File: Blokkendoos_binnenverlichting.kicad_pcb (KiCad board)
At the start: 2 copper layers, 206.8 x 26 mm, 104 parts, among them J1 Conn_01x02, J10 Conn_01x04, J11 Conn_01x04, J12 Conn_01x04, J13 Conn_01x04, J14 Conn_01x04, J15 Conn_01x04, J2 Conn_02x11_Counter_Clockwise, J3 Conn_01x04, J4 Conn_01x02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

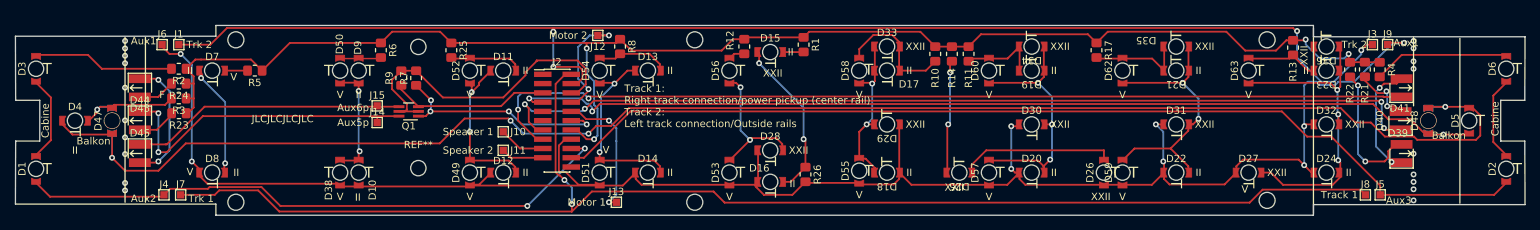
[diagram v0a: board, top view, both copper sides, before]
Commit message: Fixed mounting hole locations and sizes, closes #8
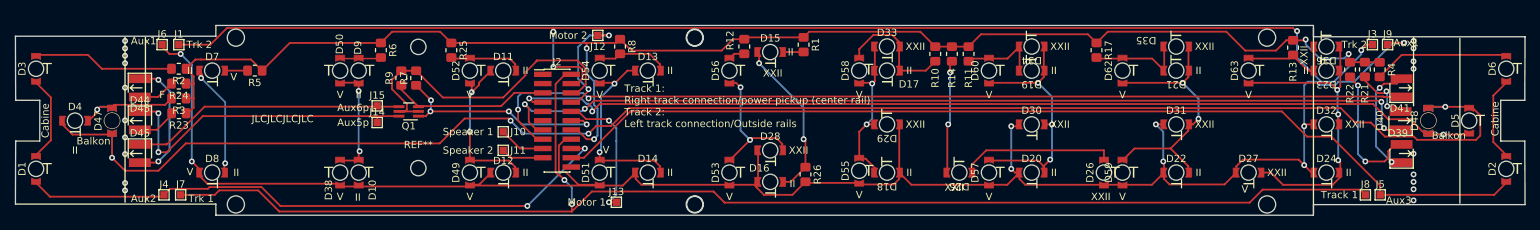
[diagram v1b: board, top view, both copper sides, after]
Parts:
- moved REF** 0.55 mm to (220.5, 138.5)
- moved REF** 0.30 mm to (220.5, 115.6)
- moved REF** 0.30 mm to (79.2, 138.5)
- moved REF** 0.30 mm to (142.1, 138.5)
- moved REF** 0.30 mm to (142.1, 115.6)
- moved REF** 0.30 mm to (79.2, 115.6)
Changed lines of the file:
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@@
   )
   (footprint "MountingHole:MountingHole_2.2mm_M2" locked (layer "F.Cu")
-    (at 220.472 115.922)
+    (at 220.472 115.624)
     (descr "Mounting Hole 2.2mm, no annular, M2")
     (tags "mounting hole 2.2mm no annular m2")
@@
     (fp_circle (center 0 0) (end 2.2 0) (layer "Cmts.User") (width 0.15) (fill none))
     (fp_circle (center 0 0) (end 2.45 0) (layer "F.CrtYd") (width 0.05) (fill none))
-    (pad "" np_thru_hole circle locked (at 0 0) (size 2.2 2.2) (drill 2.2) (layers *.Cu *.Mask))
+    (pad "" np_thru_hole circle locked (at 0 0) (size 2.35 2.35) (drill 2.35) (layers F&B.Cu *.Mask))
   )
   (footprint "Pyth:MHT151CYCT" (layer "F.Cu")
@@
   )
   (footprint "MountingHole:MountingHole_2.2mm_M2" locked (layer "F.Cu")
-    (at 79.192 138.176)
+    (at 79.192 138.474)
     (descr "Mounting Hole 2.2mm, no annular, M2")
     (tags "mounting hole 2.2mm no annular m2")
@@
     (fp_circle (center 0 0) (end 2.2 0) (layer "Cmts.User") (width 0.15) (fill none))
     (fp_circle (center 0 0) (end 2.45 0) (layer "F.CrtYd") (width 0.05) (fill none))
-    (pad "" np_thru_hole circle locked (at 0 0) (size 2.2 2.2) (drill 2.2) (layers *.Cu *.Mask))
+    (pad "" np_thru_hole circle locked (at 0 0) (size 2.35 2.35) (drill 2.35) (layers F&B.Cu *.Mask))
   )
   (footprint "Pyth:MHT151CYCT" (layer "F.Cu")
@@
   )
   (footprint "MountingHole:MountingHole_2.2mm_M2" locked (layer "F.Cu")
-    (at 142.062 138.176)
+    (at 142.062 138.474)
     (descr "Mounting Hole 2.2mm, no annular, M2")
     (tags "mounting hole 2.2mm no annular m2")
@@
     (fp_circle (center 0 0) (end 2.2 0) (layer "Cmts.User") (width 0.15) (fill none))
     (fp_circle (center 0 0) (end 2.45 0) (layer "F.CrtYd") (width 0.05) (fill none))
-    (pad "" np_thru_hole circle locked (at 0 0) (size 2.2 2.2) (drill 2.2) (layers *.Cu *.Mask))
+    (pad "" np_thru_hole circle locked (at 0 0) (size 2.35 2.35) (drill 2.35) (layers F&B.Cu *.Mask))
     (pad "" np_thru_hole circle locked (at 0 0) (size 2.2 2.2) (drill 2.2) (layers *.Cu *.Mask))
   )
@@
   )
   (footprint "MountingHole:MountingHole_2.2mm_M2" locked (layer "F.Cu")
-    (at 142.062 115.922)
+    (at 142.062 115.624)
     (descr "Mounting Hole 2.2mm, no annular, M2")
     (tags "mounting hole 2.2mm no annular m2")
@@
     (fp_circle (center 0 0) (end 2.2 0) (layer "Cmts.User") (width 0.15) (fill none))
     (fp_circle (center 0 0) (end 2.45 0) (layer "F.CrtYd") (width 0.05) (fill none))
-    (pad "" np_thru_hole circle locked (at 0 0) (size 2.2 2.2) (drill 2.2) (layers *.Cu *.Mask))
+    (pad "" np_thru_hole circle locked (at 0 0) (size 2.35 2.35) (drill 2.35) (layers F&B.Cu *.Mask))
     (pad "" np_thru_hole circle locked (at 0 0) (size 2.2 2.2) (drill 2.2) (layers *.Cu *.Mask))
   )
@@
   )
   (footprint "MountingHole:MountingHole_2.2mm_M2" locked (layer "F.Cu")
-    (at 79.192 115.922)
+    (at 79.192 115.624)
     (descr "Mounting Hole 2.2mm, no annular, M2")
     (tags "mounting hole 2.2mm no annular m2")
@@
     (fp_circle (center 0 0) (end 2.2 0) (layer "Cmts.User") (width 0.15) (fill none))
     (fp_circle (center 0 0) (end 2.45 0) (layer "F.CrtYd") (width 0.05) (fill none))
-    (pad "" np_thru_hole circle locked (at 0 0) (size 2.2 2.2) (drill 2.2) (layers *.Cu *.Mask))
+    (pad "" np_thru_hole circle locked (at 0 0) (size 2.35 2.35) (drill 2.35) (layers F&B.Cu *.Mask))
   )
   (footprint "Pyth:MHT151CYCT_dual_side" (layer "F.Cu")
@@
   )
   (footprint "MountingHole:MountingHole_2.2mm_M2" locked (layer "F.Cu")
-    (at 220.472 137.922)
+    (at 220.472 138.474)
     (descr "Mounting Hole 2.2mm, no annular, M2")
     (tags "mounting hole 2.2mm no annular m2")
@@
     (fp_circle (center 0 0) (end 2.2 0) (layer "Cmts.User") (width 0.15) (fill none))
     (fp_circle (center 0 0) (end 2.45 0) (layer "F.CrtYd") (width 0.05) (fill none))
-    (pad "" np_thru_hole circle locked (at 0 0) (size 2.2 2.2) (drill 2.2) (layers *.Cu *.Mask))
+    (pad "" np_thru_hole circle locked (at 0 0) (size 2.35 2.35) (drill 2.35) (layers F&B.Cu *.Mask))
   )
   (footprint "Pyth:MHT151CYCT" (layer "F.Cu")

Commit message: Moved motor car mounting holes, closes #7
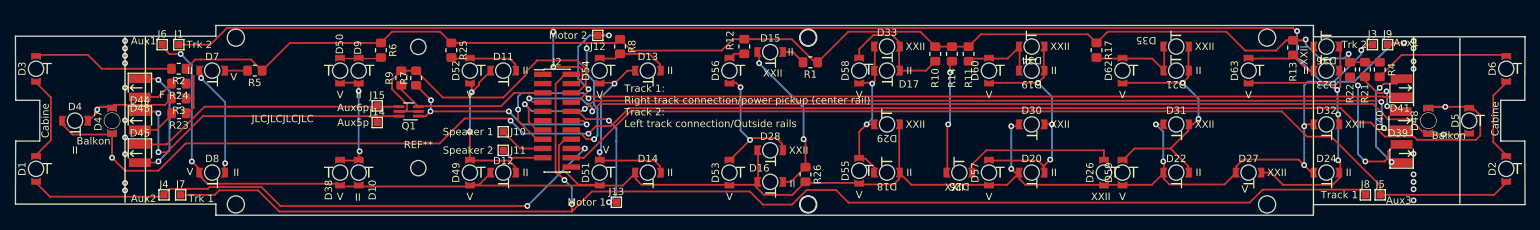
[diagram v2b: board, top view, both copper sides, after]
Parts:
- moved REF** 15.5 mm to (157.6, 138.5)
- moved REF** 15.5 mm to (157.6, 115.6)
- moved R1 2.59 mm to (157.9, 119.0), turned to 180 degrees
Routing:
- net VPP: track 203.4 -> 206.4 mm
- net /Gleis 1: track 187.7 -> 189.4 mm

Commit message: Moved front and rear light, closes #14, moved x less then 1.4 mm, that seems too much.
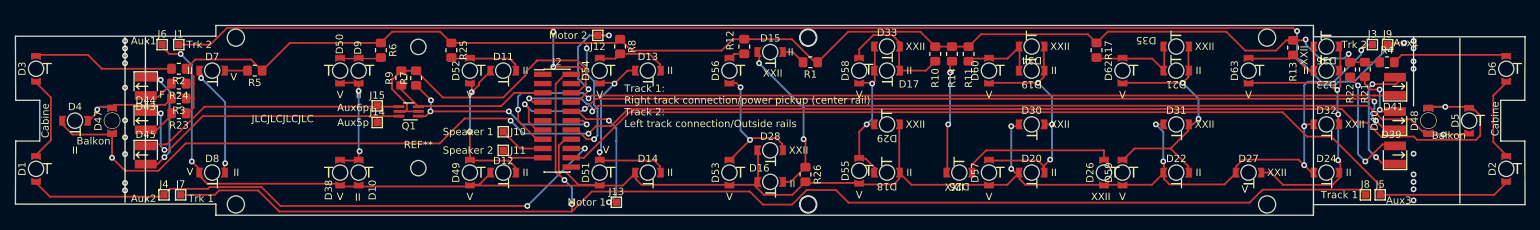
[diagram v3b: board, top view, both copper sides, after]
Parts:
- moved R4 1.41 mm to (236.9, 119.0), turned to 0 degrees
- moved D41 0.92 mm to (238.0, 122.3)
- moved D39 0.92 mm to (238.0, 131.7)
- moved D43 0.82 mm to (66.8, 122.3)
- moved D45 0.82 mm to (66.8, 131.7)
- moved D44 0.80 mm to (66.8, 127.0)
- moved D40 0.76 mm to (238.0, 127.0)
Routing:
- net Net-(D6-Pad2): track 18.6 -> 15.8 mm
- net Net-(D39-Pad1): track 16.2 -> 18.1 mm
- net /Aux5p: track 43.7 -> 42.2 mm
- net /F0r: track 129.6 -> 130.7 mm
- net /F0f: track 129.4 -> 128.5 mm
- net Net-(D43-Pad1): track 17.7 -> 16.8 mm
- net Net-(D39-Pad2): track 18.9 -> 18.4 mm

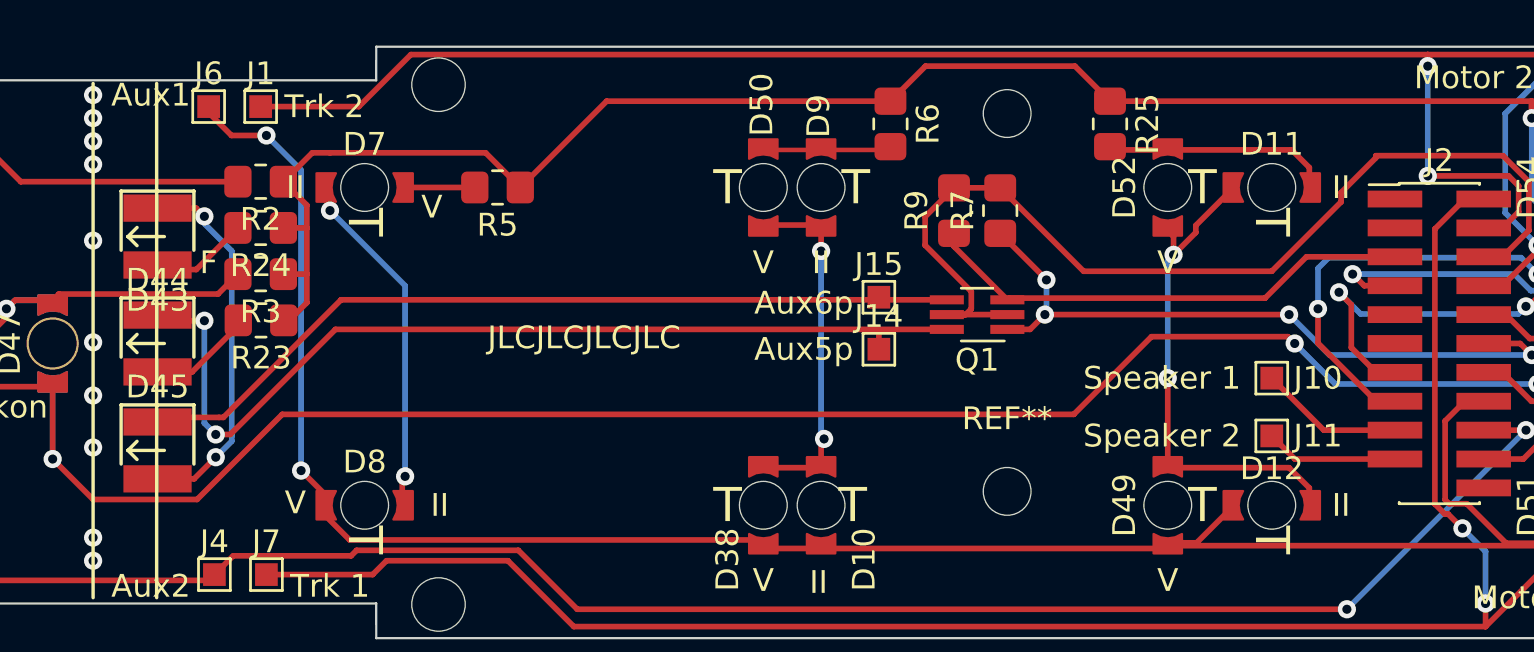
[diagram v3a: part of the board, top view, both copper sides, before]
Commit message: Removed powerpack hardware, should be on separate PCB. Replaced FDC6303, closes #12
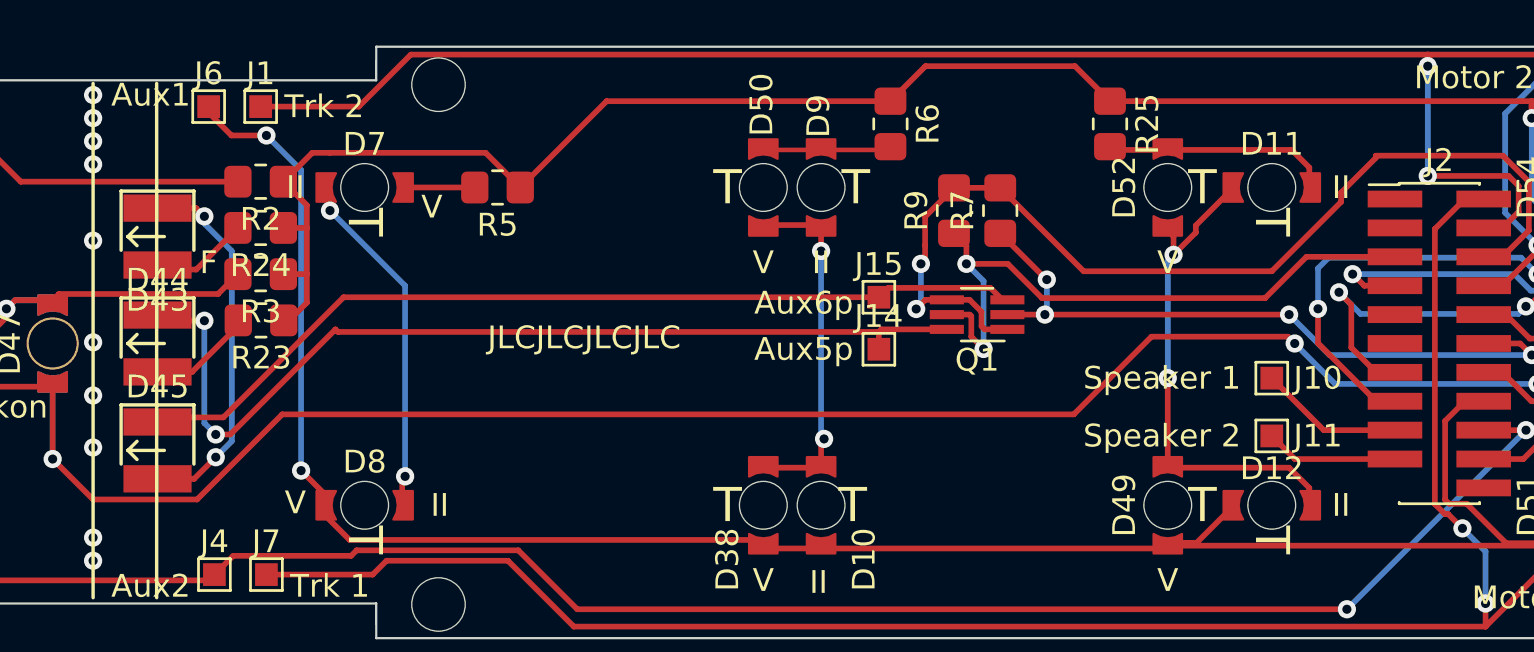
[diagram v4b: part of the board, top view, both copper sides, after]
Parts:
- removed the REF** at (104.2, 133.5)
- removed the REF** at (104.2, 116.9)
- Q1: value 21mtc-rescue_FDC6303N-mosfet_smd -> US6K1
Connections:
- Q1 pad 1: /Aux5 -> GND
- Q1 pad 2: GND -> /Aux5
- Q1 pad 3: /Aux6 -> /Aux6p
- Q1 pad 4: /Aux6p -> GND
- Q1 pad 5: GND -> /Aux6
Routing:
- net /Aux6: track 21.7 -> 28.6 mm, vias 0 -> 2
- net /Aux6p: track 37.6 -> 40.7 mm
- net GND: track 44.8 -> 45.4 mm, vias 0 -> 2

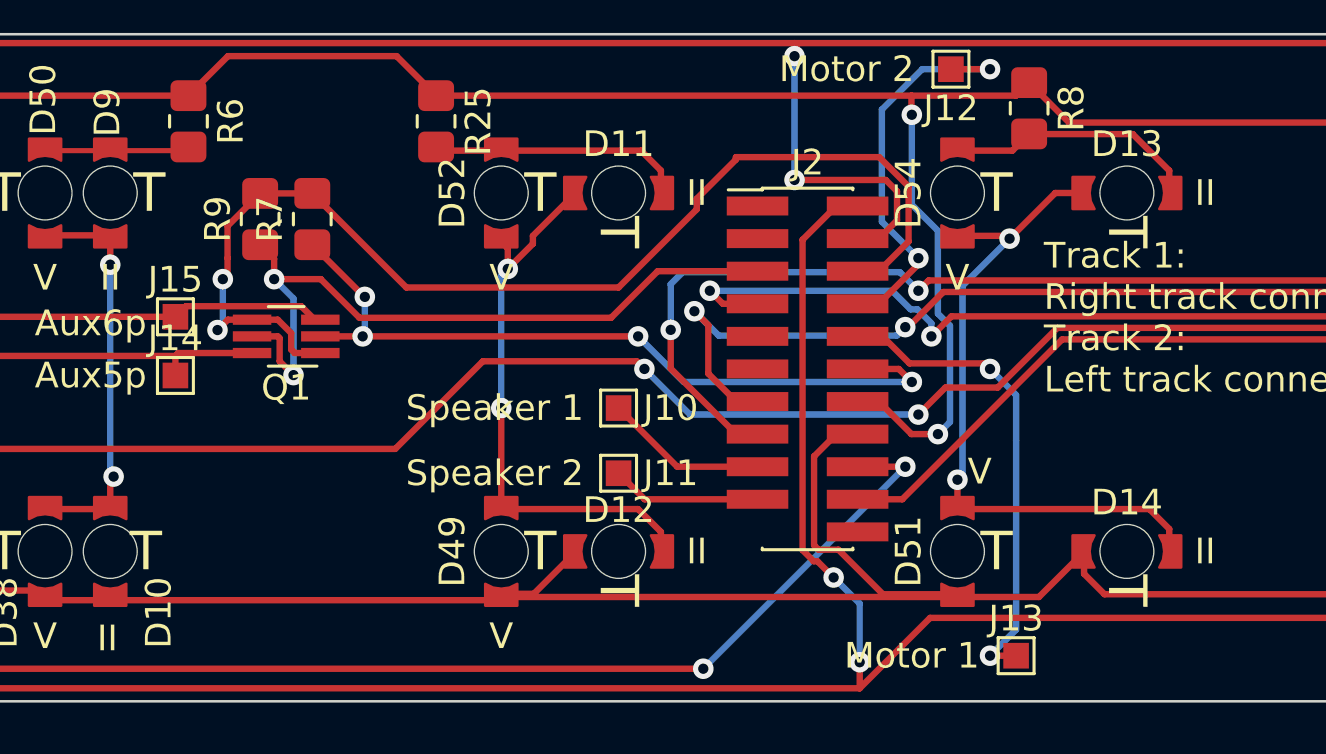
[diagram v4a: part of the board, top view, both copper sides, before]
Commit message: Added motor spring mount pads, closes #9
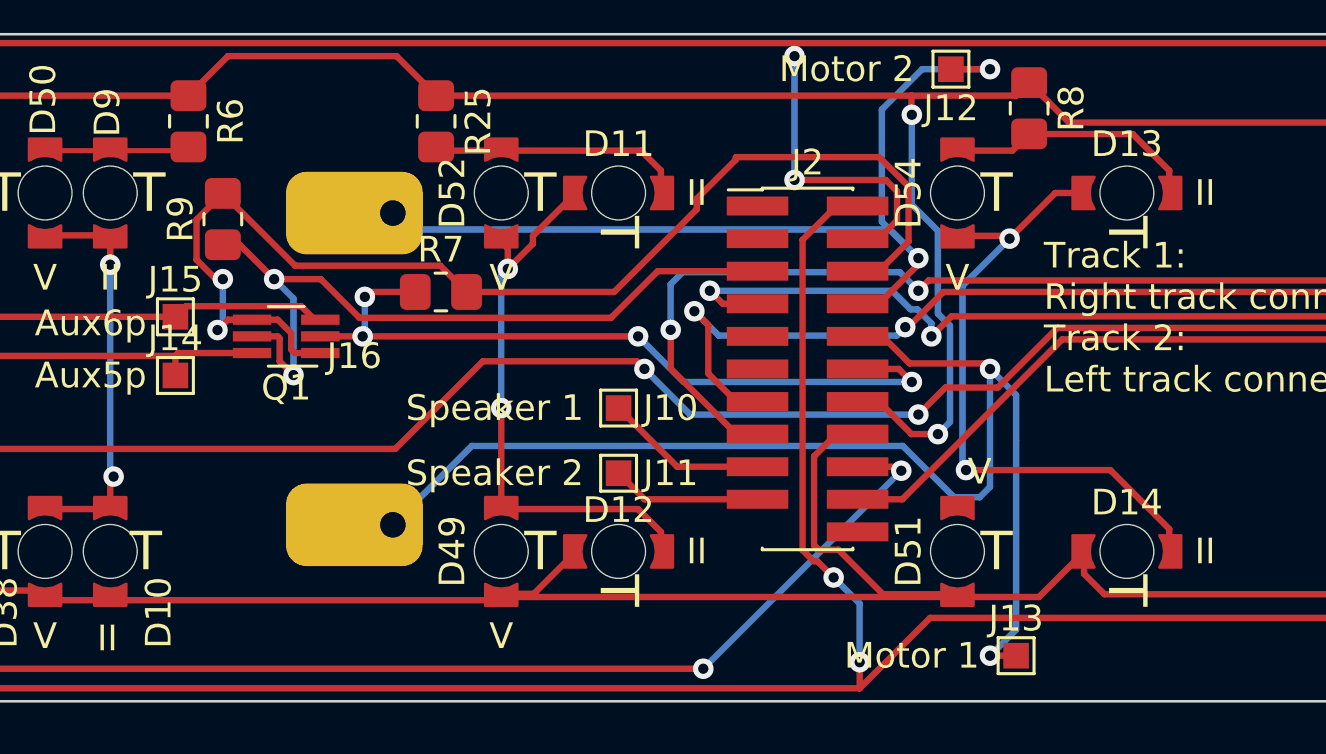
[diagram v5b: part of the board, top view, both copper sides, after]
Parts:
- added J16: Conn_01x02, Pyth:Blokkendoos motor spings, F.Cu at (105.5, 127.0)
- moved R7 5.76 mm to (108.9, 124.0), turned to 0 degrees
- moved R9 1.45 mm to (100.4, 121.2)
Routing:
- net /Motor2: track 18.7 -> 48.9 mm
- net /Motor1: track 16.0 -> 37.2 mm
- net GND: track 45.4 -> 47.4 mm
- net Net-(D13-Pad1): track 26.6 -> 25.3 mm
- net /Aux6: track 28.6 -> 29.6 mm
- net /Aux5: track 30.6 -> 29.7 mm
